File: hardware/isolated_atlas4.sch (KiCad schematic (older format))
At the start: 15 parts, among them J601 CONN_01X02, P6 ATLAS_ORP_PROBE, U601 ADM3260, U602 ATLAS_ORP

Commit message: Trying out some test points.
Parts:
- added J17, J18: CONN_01x02, conservify:TP_Pads_D1.5mm_1x2, symbol conservify:CONN_01x02
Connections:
- wire segments 78 -> 82
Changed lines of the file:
@@
 NoConn ~ 3650 3000
 NoConn ~ 5200 3000
+Text Label 8350 4500 0    60   ~ 0
+ISO_GND
+Text Label 8350 4400 0    60   ~ 0
+ISO_VCC
+Text Label 8350 4150 0    60   ~ 0
+ISO_SCL
+Text Label 8350 4250 0    60   ~ 0
+ISO_SDA
+Wire Wire Line
+	8350 4150 8750 4150
+Wire Wire Line
+	8750 4250 8350 4250
+Wire Wire Line
+	8350 4400 8750 4400
+Wire Wire Line
+	8750 4500 8350 4500
+$Comp
+L conservify:CONN_01x02 J?
+U 1 1 5C0F4248
+P 8950 4150
+AR Path="/594C282A/5C0F4248" Ref="J?"  Part="1"
+AR Path="/594C282B/5C0F4248" Ref="J17"  Part="1"
+F 0 "J17" H 9029 4142 50  0000 L CNN
+F 1 "CONN_01x02" H 9029 4051 50  0000 L CNN
+F 2 "conservify:TP_Pads_D1.5mm_1x2" H 8950 4150 50  0001 C CNN
+F 3 "" H 8950 4150 50  0001 C CNN
+	1    8950 4150
+	1    0    0    -1
+$EndComp
+$Comp
+L conservify:CONN_01x02 J?
+U 1 1 5C0F424F
+P 8950 4400
+AR Path="/594C282A/5C0F424F" Ref="J?"  Part="1"
+AR Path="/594C282B/5C0F424F" Ref="J18"  Part="1"
+F 0 "J18" H 9029 4392 50  0000 L CNN
+F 1 "CONN_01x02" H 9029 4301 50  0000 L CNN
+F 2 "conservify:TP_Pads_D1.5mm_1x2" H 8950 4400 50  0001 C CNN
+F 3 "" H 8950 4400 50  0001 C CNN
+	1    8950 4400
+	1    0    0    -1
+$EndComp
 $EndSCHEMATC

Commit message: Add orientation indicator to SWD fp.
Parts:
- J17, J18: Critical (none) -> (none); MFN (none) -> (none); MFP (none) -> (none); Notes (none) -> (none); Package (none) -> (none); SPN1 (none) -> (none); Source (none) -> ANY; Subsystem (none) -> (none); Supplier1 (none) -> (none)
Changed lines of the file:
@@
+	1    0    0    -1
+$EndComp
+$Comp
+L conservify:CONN_01x02 J?
+U 1 1 5C0F4248
+P 8950 4150
+AR Path="/594C282A/5C0F4248" Ref="J?"  Part="1"
+AR Path="/594C282B/5C0F4248" Ref="J17"  Part="1"
+F 0 "J17" H 9029 4142 50  0000 L CNN
+F 1 "CONN_01x02" H 9029 4051 50  0000 L CNN
+F 2 "conservify:TP_Pads_D1.5mm_1x2" H 8950 4150 50  0001 C CNN
+F 3 "" H 8950 4150 50  0001 C CNN
+F 4 " " H 9029 4242 50  0001 C CNN "Critical"
+F 5 " " H 9029 4242 50  0001 C CNN "MFN"
+F 6 " " H 9029 4242 50  0001 C CNN "MFP"
+F 7 " " H 9029 4242 50  0001 C CNN "Notes"
+F 8 " " H 9029 4242 50  0001 C CNN "Package"
+F 9 " " H 9029 4242 50  0001 C CNN "SPN1"
+F 10 "ANY" H 9029 4242 50  0001 C CNN "Source"
+F 11 " " H 9029 4242 50  0001 C CNN "Subsystem"
+F 12 " " H 9029 4242 50  0001 C CNN "Supplier1"
+	1    8950 4150
+	1    0    0    -1
+$EndComp
+$Comp
+L conservify:CONN_01x02 J?
+U 1 1 5C0F424F
+P 8950 4400
+AR Path="/594C282A/5C0F424F" Ref="J?"  Part="1"
+AR Path="/594C282B/5C0F424F" Ref="J18"  Part="1"
+F 0 "J18" H 9029 4392 50  0000 L CNN
+F 1 "CONN_01x02" H 9029 4301 50  0000 L CNN
+F 2 "conservify:TP_Pads_D1.5mm_1x2" H 8950 4400 50  0001 C CNN
+F 3 "" H 8950 4400 50  0001 C CNN
+F 4 " " H 9029 4492 50  0001 C CNN "Critical"
+F 5 " " H 9029 4492 50  0001 C CNN "MFN"
+F 6 " " H 9029 4492 50  0001 C CNN "MFP"
+F 7 " " H 9029 4492 50  0001 C CNN "Notes"
+F 8 " " H 9029 4492 50  0001 C CNN "Package"
+F 9 " " H 9029 4492 50  0001 C CNN "SPN1"
+F 10 "ANY" H 9029 4492 50  0001 C CNN "Source"
+F 11 " " H 9029 4492 50  0001 C CNN "Subsystem"
+F 12 " " H 9029 4492 50  0001 C CNN "Supplier1"
+	1    8950 4400
 	1    0    0    -1
 $EndComp
@@
 Text Label 9500 2900 0    60   ~ 0
 ORP_PGND
+Text Label 8350 4500 0    60   ~ 0
+ISO_GND
+Text Label 8350 4400 0    60   ~ 0
+ISO_VCC
+Text Label 8350 4150 0    60   ~ 0
+ISO_SCL
+Text Label 8350 4250 0    60   ~ 0
+ISO_SDA
 Wire Wire Line
 	5200 3300 5350 3300
@@
 Wire Wire Line
 	7400 4900 7400 5000
+Wire Wire Line
+	8350 4150 8750 4150
+Wire Wire Line
+	8750 4250 8350 4250
+Wire Wire Line
+	8350 4400 8750 4400
+Wire Wire Line
+	8750 4500 8350 4500
 Connection ~ 5350 3500
 Connection ~ 5350 3400
@@
 NoConn ~ 3650 3000
 NoConn ~ 5200 3000
-Text Label 8350 4500 0    60   ~ 0
-ISO_GND
-Text Label 8350 4400 0    60   ~ 0
-ISO_VCC
-Text Label 8350 4150 0    60   ~ 0
-ISO_SCL
-Text Label 8350 4250 0    60   ~ 0
-ISO_SDA
-Wire Wire Line
-	8350 4150 8750 4150
-Wire Wire Line
-	8750 4250 8350 4250
-Wire Wire Line
-	8350 4400 8750 4400
-Wire Wire Line
-	8750 4500 8350 4500
-$Comp
-L conservify:CONN_01x02 J?
-U 1 1 5C0F4248
-P 8950 4150
-AR Path="/594C282A/5C0F4248" Ref="J?"  Part="1"
-AR Path="/594C282B/5C0F4248" Ref="J17"  Part="1"
-F 0 "J17" H 9029 4142 50  0000 L CNN
-F 1 "CONN_01x02" H 9029 4051 50  0000 L CNN
-F 2 "conservify:TP_Pads_D1.5mm_1x2" H 8950 4150 50  0001 C CNN
-F 3 "" H 8950 4150 50  0001 C CNN
-	1    8950 4150
-	1    0    0    -1
-$EndComp
-$Comp
-L conservify:CONN_01x02 J?
-U 1 1 5C0F424F
-P 8950 4400
-AR Path="/594C282A/5C0F424F" Ref="J?"  Part="1"
-AR Path="/594C282B/5C0F424F" Ref="J18"  Part="1"
-F 0 "J18" H 9029 4392 50  0000 L CNN
-F 1 "CONN_01x02" H 9029 4301 50  0000 L CNN
-F 2 "conservify:TP_Pads_D1.5mm_1x2" H 8950 4400 50  0001 C CNN
-F 3 "" H 8950 4400 50  0001 C CNN
-	1    8950 4400
-	1    0    0    -1
-$EndComp
 $EndSCHEMATC

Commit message: Started transition to 4 layer board
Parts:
- removed J17, J18: CONN_01x02, conservify:TP_Pads_D1.5mm_1x2, symbol conservify:CONN_01x02
- C601, C602, C603, C604, C605, C606: symbol conservify:CAPACITOR_CERAMIC -> fk-atlas-rescue:CAPACITOR_CERAMIC-conservify
- J601: symbol conservify:CONN_01x02 -> fk-atlas-rescue:CONN_01x02-conservify
- P6: symbol conservify:ATLAS_WATER_PROBE -> fk-atlas-rescue:ATLAS_WATER_PROBE-conservify
- R601, R602, R603, R604, R605: symbol conservify:R -> fk-atlas-rescue:R-conservify
- U601: symbol conservify:ADM3260 -> fk-atlas-rescue:ADM3260-conservify
- U602: footprint conservify:ATLAS_SENSOR_BOARD_OEM -> conservify:ATLAS_SENSOR_BOARD_COMBO; symbol conservify:ATLAS_SENSOR -> fk-atlas-rescue:ATLAS_SENSOR-conservify
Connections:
- wire segments 82 -> 78
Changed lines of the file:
@@
 $EndDescr
 $Comp
-L conservify:ADM3260 U601
+L fk-atlas-rescue:ADM3260-conservify U601
 U 1 1 594C2CEF
 P 4400 2900
@@
 $EndComp
 $Comp
-L conservify:CAPACITOR_CERAMIC C603
+L fk-atlas-rescue:CAPACITOR_CERAMIC-conservify C603
 U 1 1 5948D4BD
 P 5650 3800
@@
 $EndComp
 $Comp
-L conservify:CAPACITOR_CERAMIC C604
+L fk-atlas-rescue:CAPACITOR_CERAMIC-conservify C604
 U 1 1 594C2CFA
 P 5650 4100
@@
 $EndComp
 $Comp
-L conservify:CAPACITOR_CERAMIC C605
+L fk-atlas-rescue:CAPACITOR_CERAMIC-conservify C605
 U 1 1 594C2CFD
 P 5650 4400
@@
 $EndComp
 $Comp
-L conservify:CAPACITOR_CERAMIC C606
+L fk-atlas-rescue:CAPACITOR_CERAMIC-conservify C606
 U 1 1 5948D5D0
 P 5650 4650
@@
 $EndComp
 $Comp
-L conservify:CAPACITOR_CERAMIC C601
+L fk-atlas-rescue:CAPACITOR_CERAMIC-conservify C601
 U 1 1 594C2D05
 P 2900 3800
@@
 $EndComp
 $Comp
-L conservify:CAPACITOR_CERAMIC C602
+L fk-atlas-rescue:CAPACITOR_CERAMIC-conservify C602
 U 1 1 594C2D0A
 P 2900 4100
@@
 $EndComp
 $Comp
-L conservify:R R601
+L fk-atlas-rescue:R-conservify R601
 U 1 1 5948D6B5
 P 5650 3300
@@
 $EndComp
 $Comp
-L conservify:R R602
+L fk-atlas-rescue:R-conservify R602
 U 1 1 5948E326
 P 6250 2700
@@
 $EndComp
 $Comp
-L conservify:R R604
+L fk-atlas-rescue:R-conservify R604
 U 1 1 594C2D13
 P 6700 2700
@@
 $EndComp
 $Comp
-L conservify:R R603
+L fk-atlas-rescue:R-conservify R603
 U 1 1 594C2D18
 P 6300 3250
@@
 $EndComp
 $Comp
-L conservify:R R605
+L fk-atlas-rescue:R-conservify R605
 U 1 1 594C2D1C
 P 6800 3250
@@
 $EndComp
 $Comp
-L conservify:VCC #PWR065
+L fk-atlas-rescue:VCC-conservify #PWR065
 U 1 1 594C2D25
 P 2450 3750
@@
 $EndComp
 $Comp
-L conservify:VCC #PWR066
+L fk-atlas-rescue:VCC-conservify #PWR066
 U 1 1 594C2D27
 P 2450 2350
@@
 $EndComp
 $Comp
-L conservify:ATLAS_SENSOR U602
+L fk-atlas-rescue:ATLAS_SENSOR-conservify U602
 U 1 1 594C1D09
 P 8550 2900
 F 0 "U602" H 8100 2550 60  0000 C CNN
 F 1 "ATLAS_ORP" H 8600 2850 60  0000 C CNN
-F 2 "conservify:ATLAS_SENSOR_BOARD_OEM" H 8550 2900 60  0001 C CNN
+F 2 "conservify:ATLAS_SENSOR_BOARD_COMBO" H 8550 2900 60  0001 C CNN
 F 3 "" H 8550 2900 60  0001 C CNN
 F 4 " " H 8100 2650 50  0001 C CNN "Critical"
@@
 $EndComp
 $Comp
-L conservify:CONN_01x02 J601
+L fk-atlas-rescue:CONN_01x02-conservify J601
 U 1 1 59A1BC7E
 P 10200 2900
@@
 $EndComp
 $Comp
-L conservify:ATLAS_WATER_PROBE P6
+L fk-atlas-rescue:ATLAS_WATER_PROBE-conservify P6
 U 1 1 59D2AB5D
 P 8800 3600
@@
 $EndComp
 $Comp
-L conservify:PWR_FLAG #FLG0109
+L fk-atlas-rescue:PWR_FLAG-conservify #FLG0109
 U 1 1 5BCDD0A6
 P 7400 4900
@@
 F 3 "~" H 7400 4900 50  0001 C CNN
 	1    7400 4900
-	1    0    0    -1
-$EndComp
-$Comp
-L conservify:CONN_01x02 J?
-U 1 1 5C0F4248
-P 8950 4150
-AR Path="/594C282A/5C0F4248" Ref="J?"  Part="1"
-AR Path="/594C282B/5C0F4248" Ref="J17"  Part="1"
-F 0 "J17" H 9029 4142 50  0000 L CNN
-F 1 "CONN_01x02" H 9029 4051 50  0000 L CNN
-F 2 "conservify:TP_Pads_D1.5mm_1x2" H 8950 4150 50  0001 C CNN
-F 3 "" H 8950 4150 50  0001 C CNN
-F 4 " " H 9029 4242 50  0001 C CNN "Critical"
-F 5 " " H 9029 4242 50  0001 C CNN "MFN"
-F 6 " " H 9029 4242 50  0001 C CNN "MFP"
-F 7 " " H 9029 4242 50  0001 C CNN "Notes"
-F 8 " " H 9029 4242 50  0001 C CNN "Package"
-F 9 " " H 9029 4242 50  0001 C CNN "SPN1"
-F 10 "ANY" H 9029 4242 50  0001 C CNN "Source"
-F 11 " " H 9029 4242 50  0001 C CNN "Subsystem"
-F 12 " " H 9029 4242 50  0001 C CNN "Supplier1"
-	1    8950 4150
-	1    0    0    -1
-$EndComp
-$Comp
-L conservify:CONN_01x02 J?
-U 1 1 5C0F424F
-P 8950 4400
-AR Path="/594C282A/5C0F424F" Ref="J?"  Part="1"
-AR Path="/594C282B/5C0F424F" Ref="J18"  Part="1"
-F 0 "J18" H 9029 4392 50  0000 L CNN
-F 1 "CONN_01x02" H 9029 4301 50  0000 L CNN
-F 2 "conservify:TP_Pads_D1.5mm_1x2" H 8950 4400 50  0001 C CNN
-F 3 "" H 8950 4400 50  0001 C CNN
-F 4 " " H 9029 4492 50  0001 C CNN "Critical"
-F 5 " " H 9029 4492 50  0001 C CNN "MFN"
-F 6 " " H 9029 4492 50  0001 C CNN "MFP"
-F 7 " " H 9029 4492 50  0001 C CNN "Notes"
-F 8 " " H 9029 4492 50  0001 C CNN "Package"
-F 9 " " H 9029 4492 50  0001 C CNN "SPN1"
-F 10 "ANY" H 9029 4492 50  0001 C CNN "Source"
-F 11 " " H 9029 4492 50  0001 C CNN "Subsystem"
-F 12 " " H 9029 4492 50  0001 C CNN "Supplier1"
-	1    8950 4400
 	1    0    0    -1
 $EndComp
@@
 Text Label 9500 2900 0    60   ~ 0
 ORP_PGND
-Text Label 8350 4500 0    60   ~ 0
-ISO_GND
-Text Label 8350 4400 0    60   ~ 0
-ISO_VCC
-Text Label 8350 4150 0    60   ~ 0
-ISO_SCL
-Text Label 8350 4250 0    60   ~ 0
-ISO_SDA
 Wire Wire Line
 	5200 3300 5350 3300
@@
 Wire Wire Line
 	7400 4900 7400 5000
-Wire Wire Line
-	8350 4150 8750 4150
-Wire Wire Line
-	8750 4250 8350 4250
-Wire Wire Line
-	8350 4400 8750 4400
-Wire Wire Line
-	8750 4500 8350 4500
 Connection ~ 5350 3500
 Connection ~ 5350 3400

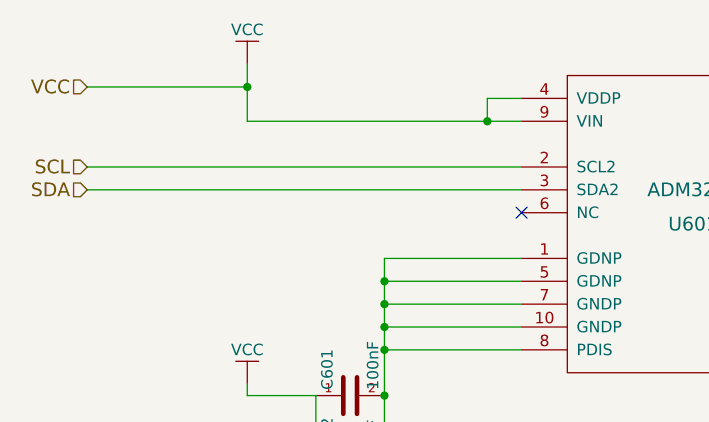
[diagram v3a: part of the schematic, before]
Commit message: Added pull up resistors and a debounce cap for the reset button
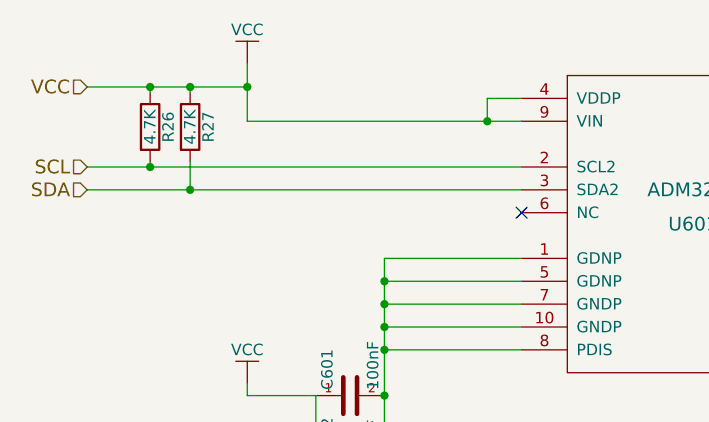
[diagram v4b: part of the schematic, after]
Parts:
- added R26, R27: 4.7K, conservify:RES-0603, symbol fk-atlas-rescue:R-conservify
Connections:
- net SCL: now also R26.2
- net SDA: now also R27.2
- net VCC: now also R26.1, R27.1
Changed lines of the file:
@@
 	2450 3800 2450 3750
 Wire Wire Line
-	1750 2800 3650 2800
+	1750 2800 2025 2800
 Wire Wire Line
-	1750 2900 3650 2900
+	1750 2900 2200 2900
 Wire Wire Line
-	1750 2450 2450 2450
+	1750 2450 2025 2450
 Wire Wire Line
 	5350 5000 7400 5000
@@
 NoConn ~ 3650 3000
 NoConn ~ 5200 3000
+$Comp
+L fk-atlas-rescue:R-conservify R26
+U 1 1 5C807DB9
+P 2025 2625
+F 0 "R26" V 2105 2625 50  0000 C CNN
+F 1 "4.7K" V 2025 2625 50  0000 C CNN
+F 2 "conservify:RES-0603" V 1955 2625 50  0001 C CNN
+F 3 "" H 2025 2625 50  0001 C CNN
+F 4 " " H 2105 2725 50  0001 C CNN "Critical"
+F 5 "Yageo" H 2105 2725 50  0001 C CNN "MFN"
+F 6 "AF0603JR-074K7L" H 2105 2725 50  0001 C CNN "MFP"
+F 7 " " H 2105 2725 50  0001 C CNN "Notes"
+F 8 " " H 2105 2725 50  0001 C CNN "Package"
+F 9 "ANY" H 2105 2725 50  0001 C CNN "Source"
+F 10 " " H 2105 2725 50  0001 C CNN "Subsystem"
+F 11 "mouser" H 2105 2725 50  0001 C CNN "Supplier1"
+F 12 "0" H 2105 2725 50  0001 C CNN "price"
+F 13 "603-AF0603JR-074K7L" H -4275 -625 50  0001 C CNN "spn1"
+F 14 "mouser" H -4275 -625 50  0001 C CNN "spn2"
+	1    2025 2625
+	1    0    0    -1
+$EndComp
+Wire Wire Line
+	2025 2475 2025 2450
+Connection ~ 2025 2450
+Wire Wire Line
+	2025 2450 2200 2450
+Wire Wire Line
+	2025 2775 2025 2800
+Connection ~ 2025 2800
+Wire Wire Line
+	2025 2800 3650 2800
+$Comp
+L fk-atlas-rescue:R-conservify R27
+U 1 1 5C80B8A0
+P 2200 2625
+F 0 "R27" V 2280 2625 50  0000 C CNN
+F 1 "4.7K" V 2200 2625 50  0000 C CNN
+F 2 "conservify:RES-0603" V 2130 2625 50  0001 C CNN
+F 3 "" H 2200 2625 50  0001 C CNN
+F 4 " " H 2280 2725 50  0001 C CNN "Critical"
+F 5 "Yageo" H 2280 2725 50  0001 C CNN "MFN"
+F 6 "AF0603JR-074K7L" H 2280 2725 50  0001 C CNN "MFP"
+F 7 " " H 2280 2725 50  0001 C CNN "Notes"
+F 8 " " H 2280 2725 50  0001 C CNN "Package"
+F 9 "ANY" H 2280 2725 50  0001 C CNN "Source"
+F 10 " " H 2280 2725 50  0001 C CNN "Subsystem"
+F 11 "mouser" H 2280 2725 50  0001 C CNN "Supplier1"
+F 12 "0" H 2280 2725 50  0001 C CNN "price"
+F 13 "603-AF0603JR-074K7L" H -4100 -625 50  0001 C CNN "spn1"
+F 14 "mouser" H -4100 -625 50  0001 C CNN "spn2"
+	1    2200 2625
+	1    0    0    -1
+$EndComp
+Wire Wire Line
+	2200 2475 2200 2450
+Connection ~ 2200 2450
+Wire Wire Line
+	2200 2450 2450 2450
+Wire Wire Line
+	2200 2775 2200 2900
+Connection ~ 2200 2900
+Wire Wire Line
+	2200 2900 3650 2900
 $EndSCHEMATC
